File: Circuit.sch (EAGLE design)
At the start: 132 parts, among them IC1 LM1117T-3.3-V, U1 MAG3110, U2 MAG3110

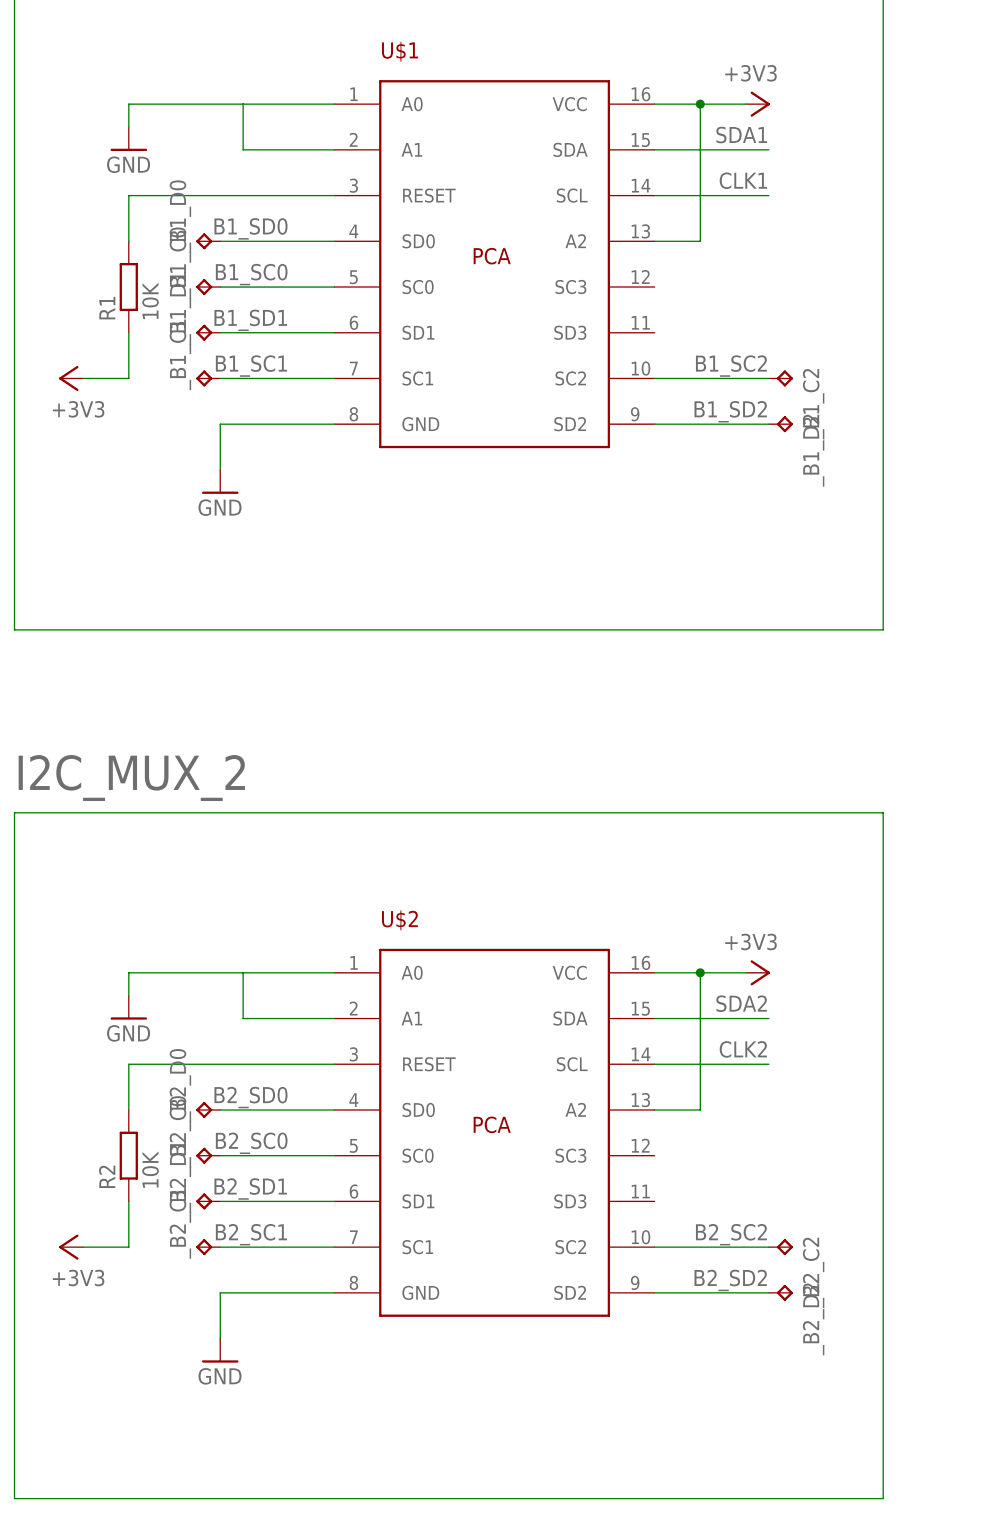
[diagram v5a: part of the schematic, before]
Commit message: Removed the test pads
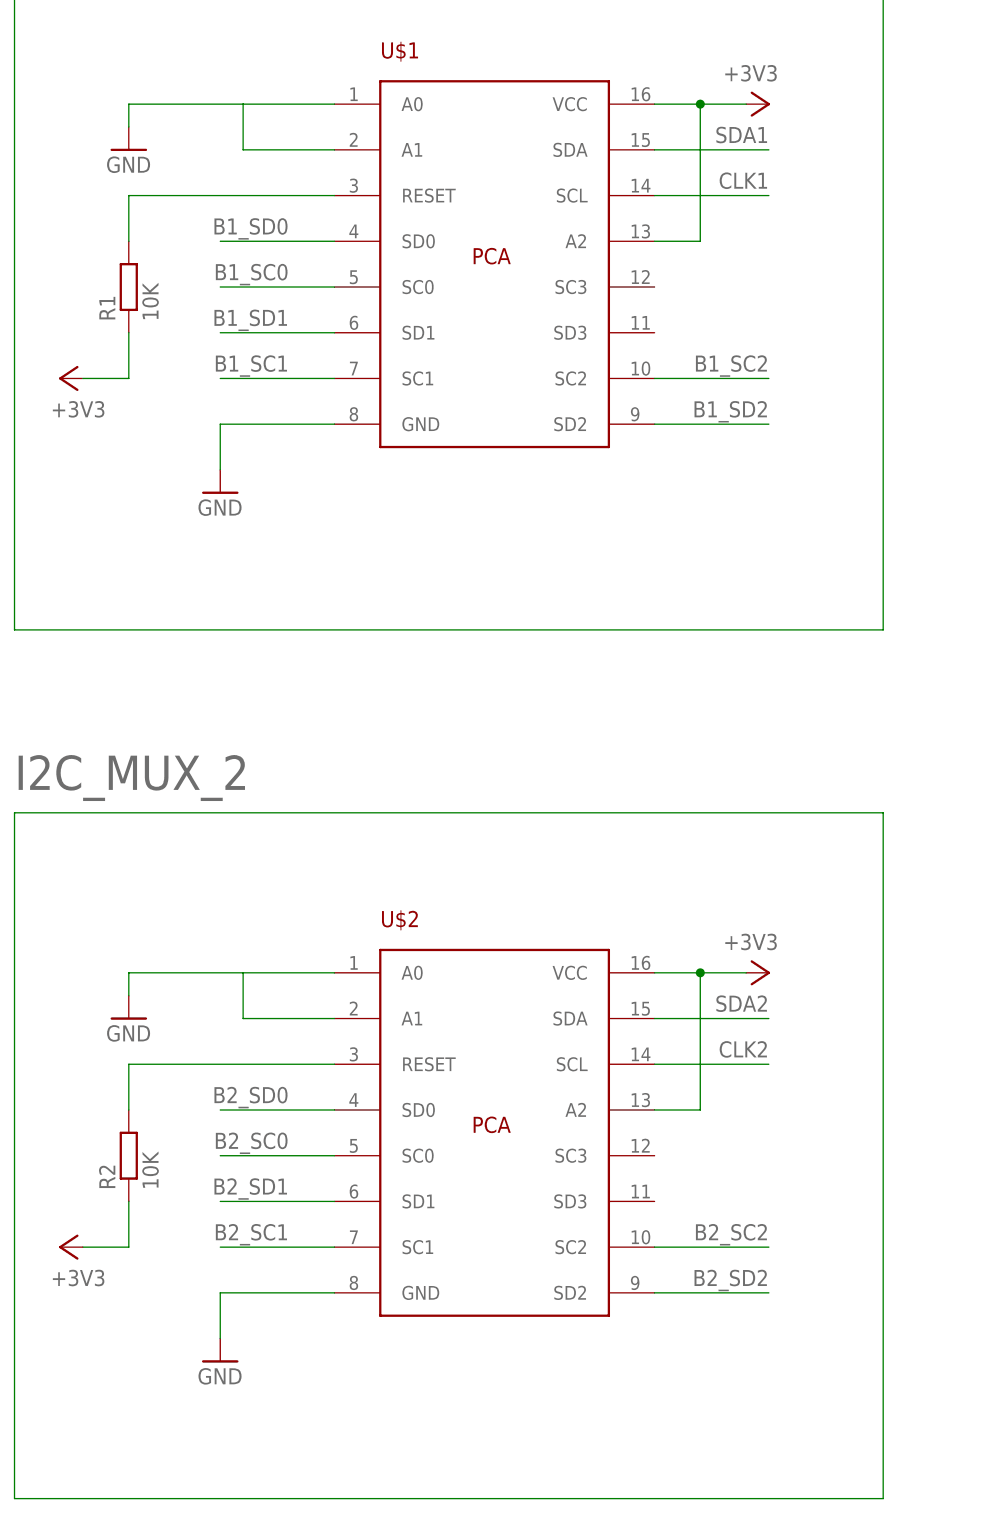
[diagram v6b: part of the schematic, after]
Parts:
- removed _B1_C0, _B1_C1, _B1_C2, _B1_D0, _B1_D1, _B1_D2, _B2_C0, _B2_C1, _B2_C2, _B2_D0, _B2_D1, _B2_D2: TPB1,27, testpad:TPB1,27
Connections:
- net B1_SC0: no longer _B1_C0.TP
- net B1_SC1: no longer _B1_C1.TP
- net B1_SC2: no longer _B1_C2.TP
- net B1_SD0: no longer _B1_D0.TP
- net B1_SD1: no longer _B1_D1.TP
- net B1_SD2: no longer _B1_D2.TP
- net B2_SC0: no longer _B2_C0.TP
- net B2_SC1: no longer _B2_C1.TP
- net B2_SC2: no longer _B2_C2.TP
- net B2_SD0: no longer _B2_D0.TP
- net B2_SD1: no longer _B2_D1.TP
- net B2_SD2: no longer _B2_D2.TP
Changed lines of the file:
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@@
 <part name="R29" library="resistor" deviceset="R-EU_" device="R0603" value="2.2K"/>
 <part name="+3V51" library="supply1" deviceset="+3V3" device=""/>
-<part name="_B1_D0" library="testpad" deviceset="TP" device="B1,27"/>
-<part name="_B1_C0" library="testpad" deviceset="TP" device="B1,27"/>
-<part name="_B1_D1" library="testpad" deviceset="TP" device="B1,27"/>
-<part name="_B1_C1" library="testpad" deviceset="TP" device="B1,27"/>
-<part name="_B1_C2" library="testpad" deviceset="TP" device="B1,27"/>
-<part name="_B1_D2" library="testpad" deviceset="TP" device="B1,27"/>
-<part name="_B2_D0" library="testpad" deviceset="TP" device="B1,27"/>
-<part name="_B2_C0" library="testpad" deviceset="TP" device="B1,27"/>
-<part name="_B2_D1" library="testpad" deviceset="TP" device="B1,27"/>
-<part name="_B2_C1" library="testpad" deviceset="TP" device="B1,27"/>
-<part name="_B2_C2" library="testpad" deviceset="TP" device="B1,27"/>
-<part name="_B2_D2" library="testpad" deviceset="TP" device="B1,27"/>
 </parts>
 <sheets>
@@
 <instance part="R29" gate="G$1" x="220.98" y="152.4" rot="R180"/>
 <instance part="+3V51" gate="G$1" x="246.38" y="160.02" rot="R270"/>
-<instance part="_B1_D0" gate="G$1" x="-198.12" y="325.12" rot="R90"/>
-<instance part="_B1_C0" gate="G$1" x="-198.12" y="320.04" rot="R90"/>
-<instance part="_B1_D1" gate="G$1" x="-198.12" y="314.96" rot="R90"/>
-<instance part="_B1_C1" gate="G$1" x="-198.12" y="309.88" rot="R90"/>
-<instance part="_B1_C2" gate="G$1" x="-132.08" y="309.88" rot="R270"/>
-<instance part="_B1_D2" gate="G$1" x="-132.08" y="304.8" rot="R270"/>
-<instance part="_B2_D0" gate="G$1" x="-198.12" y="228.6" rot="R90"/>
-<instance part="_B2_C0" gate="G$1" x="-198.12" y="223.52" rot="R90"/>
-<instance part="_B2_D1" gate="G$1" x="-198.12" y="218.44" rot="R90"/>
-<instance part="_B2_C1" gate="G$1" x="-198.12" y="213.36" rot="R90"/>
-<instance part="_B2_C2" gate="G$1" x="-132.08" y="213.36" rot="R270"/>
-<instance part="_B2_D2" gate="G$1" x="-132.08" y="208.28" rot="R270"/>
 </instances>
 <busses>
@@
 <wire x1="-182.88" y1="325.12" x2="-195.58" y2="325.12" width="0.1524" layer="91"/>
 <label x="-187.96" y="327.66" size="1.778" layer="95" rot="R180"/>
-<pinref part="_B1_D0" gate="G$1" pin="TP"/>
 </segment>
 <segment>
@@
 <wire x1="-182.88" y1="320.04" x2="-195.58" y2="320.04" width="0.1524" layer="91"/>
 <label x="-187.96" y="322.58" size="1.778" layer="95" rot="R180"/>
-<pinref part="_B1_C0" gate="G$1" pin="TP"/>
 </segment>
 <segment>
@@
 <wire x1="-182.88" y1="314.96" x2="-195.58" y2="314.96" width="0.1524" layer="91"/>
 <label x="-187.96" y="317.5" size="1.778" layer="95" rot="R180"/>
-<pinref part="_B1_D1" gate="G$1" pin="TP"/>
 </segment>
 <segment>
@@
 <wire x1="-182.88" y1="309.88" x2="-195.58" y2="309.88" width="0.1524" layer="91"/>
 <label x="-187.96" y="312.42" size="1.778" layer="95" rot="R180"/>
-<pinref part="_B1_C1" gate="G$1" pin="TP"/>
 </segment>
 <segment>
@@
 <wire x1="-147.32" y1="309.88" x2="-134.62" y2="309.88" width="0.1524" layer="91"/>
 <label x="-134.62" y="312.42" size="1.778" layer="95" rot="R180"/>
-<pinref part="_B1_C2" gate="G$1" pin="TP"/>
 </segment>
 <segment>
@@
 <wire x1="-147.32" y1="304.8" x2="-134.62" y2="304.8" width="0.1524" layer="91"/>
 <label x="-134.62" y="307.34" size="1.778" layer="95" rot="R180"/>
-<pinref part="_B1_D2" gate="G$1" pin="TP"/>
 </segment>
 <segment>
@@
 <wire x1="-182.88" y1="228.6" x2="-195.58" y2="228.6" width="0.1524" layer="91"/>
 <label x="-187.96" y="231.14" size="1.778" layer="95" rot="R180"/>
-<pinref part="_B2_D0" gate="G$1" pin="TP"/>
 </segment>
 <segment>
@@
 <wire x1="-182.88" y1="223.52" x2="-195.58" y2="223.52" width="0.1524" layer="91"/>
 <label x="-187.96" y="226.06" size="1.778" layer="95" rot="R180"/>
-<pinref part="_B2_C0" gate="G$1" pin="TP"/>
 </segment>
 <segment>
@@
 <wire x1="-182.88" y1="218.44" x2="-195.58" y2="218.44" width="0.1524" layer="91"/>
 <label x="-187.96" y="220.98" size="1.778" layer="95" rot="R180"/>
-<pinref part="_B2_D1" gate="G$1" pin="TP"/>
 </segment>
 <segment>
@@
 <wire x1="-182.88" y1="213.36" x2="-195.58" y2="213.36" width="0.1524" layer="91"/>
 <label x="-187.96" y="215.9" size="1.778" layer="95" rot="R180"/>
-<pinref part="_B2_C1" gate="G$1" pin="TP"/>
 </segment>
 <segment>
@@
 <wire x1="-147.32" y1="213.36" x2="-134.62" y2="213.36" width="0.1524" layer="91"/>
 <label x="-134.62" y="215.9" size="1.778" layer="95" rot="R180"/>
-<pinref part="_B2_C2" gate="G$1" pin="TP"/>
 </segment>
 <segment>
@@
 <wire x1="-147.32" y1="208.28" x2="-134.62" y2="208.28" width="0.1524" layer="91"/>
 <label x="-134.62" y="210.82" size="1.778" layer="95" rot="R180"/>
-<pinref part="_B2_D2" gate="G$1" pin="TP"/>
-</segment>
-<segment>
+</segment>
+<segment>

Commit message: First side 80% of 90%. Not that far in total :/
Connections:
- net B1_SC2: now also R20.2
- net B1_SD2: now also R21.2
- net CLK1: no longer R20.2
- net SDA1: no longer R21.2
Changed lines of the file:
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@@
-</segment>
-<segment>
-<pinref part="R20" gate="G$1" pin="2"/>
-<wire x1="78.74" y1="53.34" x2="76.2" y2="53.34" width="0.1524" layer="91"/>
-<wire x1="76.2" y1="53.34" x2="76.2" y2="38.1" width="0.1524" layer="91"/>
 </segment>
 <segment>
@@
 <wire x1="375.92" y1="195.58" x2="363.22" y2="195.58" width="0.1524" layer="91"/>
 <label x="363.22" y="195.58" size="1.778" layer="95"/>
-</segment>
-<segment>
-<pinref part="R21" gate="G$1" pin="2"/>
-<wire x1="86.36" y1="48.26" x2="81.28" y2="48.26" width="0.1524" layer="91"/>
-<wire x1="81.28" y1="48.26" x2="81.28" y2="35.56" width="0.1524" layer="91"/>
 </segment>
 <segment>
@@
 <net name="N$39" class="0">
 <segment>
-<wire x1="-33.02" y1="22.86" x2="-33.02" y2="25.4" width="0.1524" layer="91"/>
 <pinref part="C15" gate="G$1" pin="1"/>
+<wire x1="-38.1" y1="25.4" x2="-33.02" y2="25.4" width="0.1524" layer="91"/>
 <wire x1="-33.02" y1="25.4" x2="-22.86" y2="25.4" width="0.1524" layer="91"/>
 <wire x1="-22.86" y1="25.4" x2="-22.86" y2="22.86" width="0.1524" layer="91"/>
-<pinref part="C12" gate="G$1" pin="1"/>
 <pinref part="L3G_1" gate="G$1" pin="PLL"/>
 <wire x1="-40.64" y1="17.78" x2="-38.1" y2="17.78" width="0.1524" layer="91"/>
 <wire x1="-38.1" y1="17.78" x2="-38.1" y2="25.4" width="0.1524" layer="91"/>
-<wire x1="-38.1" y1="25.4" x2="-33.02" y2="25.4" width="0.1524" layer="91"/>
+<pinref part="C12" gate="G$1" pin="1"/>
+<wire x1="-33.02" y1="22.86" x2="-33.02" y2="25.4" width="0.1524" layer="91"/>
+<junction x="-33.02" y="25.4"/>
 </segment>
 </net>
@@
 <wire x1="76.2" y1="17.78" x2="76.2" y2="25.4" width="0.1524" layer="91"/>
 <wire x1="76.2" y1="25.4" x2="81.28" y2="25.4" width="0.1524" layer="91"/>
+<junction x="81.28" y="25.4"/>
 </segment>
 </net>
@@
 <wire x1="190.5" y1="17.78" x2="190.5" y2="25.4" width="0.1524" layer="91"/>
 <wire x1="190.5" y1="25.4" x2="195.58" y2="25.4" width="0.1524" layer="91"/>
+<junction x="195.58" y="25.4"/>
 </segment>
 </net>
@@
 <wire x1="304.8" y1="17.78" x2="304.8" y2="25.4" width="0.1524" layer="91"/>
 <wire x1="304.8" y1="25.4" x2="309.88" y2="25.4" width="0.1524" layer="91"/>
+<junction x="309.88" y="25.4"/>
 </segment>
 </net>
@@
 </segment>
 <segment>
-<pinref part="L3G_2" gate="G$1" pin="SCL"/>
-<wire x1="73.66" y1="38.1" x2="93.98" y2="38.1" width="0.1524" layer="91"/>
-<label x="93.98" y="40.64" size="1.778" layer="95" rot="R180"/>
-</segment>
-<segment>
 <pinref part="U1" gate="G$1" pin="SCL"/>
 <wire x1="-154.94" y1="124.46" x2="-144.78" y2="124.46" width="0.1524" layer="91"/>
@@
 <label x="-142.24" y="121.92" size="1.778" layer="95"/>
 </segment>
+<segment>
+<pinref part="R20" gate="G$1" pin="2"/>
+<wire x1="78.74" y1="53.34" x2="76.2" y2="53.34" width="0.1524" layer="91"/>
+<wire x1="76.2" y1="53.34" x2="76.2" y2="38.1" width="0.1524" layer="91"/>
+<pinref part="L3G_2" gate="G$1" pin="SCL"/>
+<wire x1="73.66" y1="38.1" x2="76.2" y2="38.1" width="0.1524" layer="91"/>
+<label x="93.98" y="40.64" size="1.778" layer="95" rot="R180"/>
+<junction x="76.2" y="38.1"/>
+<wire x1="76.2" y1="38.1" x2="93.98" y2="38.1" width="0.1524" layer="91"/>
+</segment>
 </net>
 <net name="B1_SD2" class="0">
@@
 <wire x1="-147.32" y1="304.8" x2="-134.62" y2="304.8" width="0.1524" layer="91"/>
 <label x="-134.62" y="307.34" size="1.778" layer="95" rot="R180"/>
-</segment>
-<segment>
-<pinref part="L3G_2" gate="G$1" pin="SDA/SDI"/>
-<wire x1="73.66" y1="35.56" x2="93.98" y2="35.56" width="0.1524" layer="91"/>
-<label x="93.98" y="38.1" size="1.778" layer="95" rot="R180"/>
 </segment>
 <segment>
@@
 <label x="-152.4" y="127" size="1.778" layer="95"/>
 </segment>
-</net>
+<segment>
+<pinref part="R21" gate="G$1" pin="2"/>
+<wire x1="86.36" y1="48.26" x2="81.28" y2="48.26" width="0.1524" layer="91"/>
+<wire x1="81.28" y1="48.26" x2="81.28" y2="35.56" width="0.1524" layer="91"/>
+<pinref part="L3G_2" gate="G$1" pin="SDA/SDI"/>
+<wire x1="73.66" y1="35.56" x2="81.28" y2="35.56" width="0.1524" layer="91"/>
+<label x="93.98" y="38.1" size="1.778" layer="95" rot="R180"/>
+<junction x="81.28" y="35.56"/>
+<wire x1="81.28" y1="35.56" x2="93.98" y2="35.56" width="0.1524" layer="91"/>
+</segment>
+</net>

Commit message: Stashing prior to optimisation of resistors
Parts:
- renumbered U$1 to MUX1, U$2 to MUX2, U1 to MAG1, U2 to MAG2
